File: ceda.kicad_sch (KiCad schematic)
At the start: 6 parts

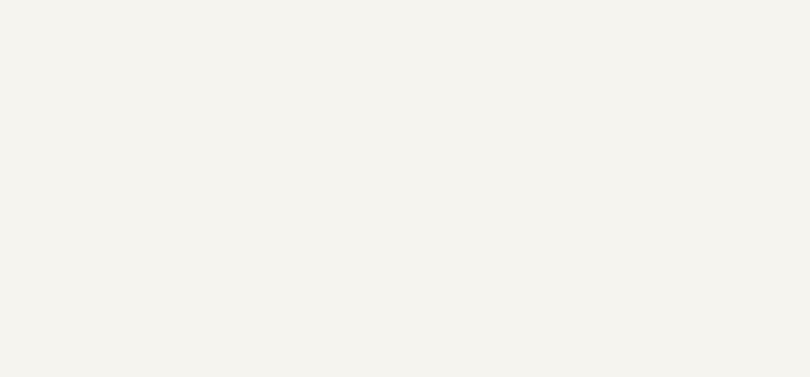
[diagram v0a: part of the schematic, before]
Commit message: CEDA symbol library: CRTC and uPD446.
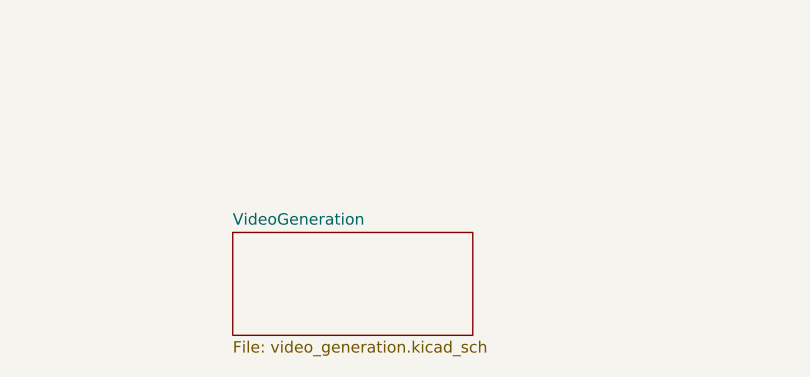
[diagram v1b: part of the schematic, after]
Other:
- added sheet VideoGeneration (video_generation.kicad_sch)
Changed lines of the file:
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@@
     (pin "2")
+  )
+  (sheet (at 36.83 153.67) (size 26.67 11.43) (fields_autoplaced)
+    (stroke (width 0.1524) (type solid) (color 0 0 0 0))
+    (fill (color 0 0 0 0.0000))
+    (property "Sheet name" "VideoGeneration" (id 0) (at 36.83 152.9584 0)
+      (effects (font (size 1.27 1.27)) (justify left bottom))
+    )
+    (property "Sheet file" "video_generation.kicad_sch" (id 1) (at 36.83 165.6846 0)
+      (effects (font (size 1.27 1.27)) (justify left top))
+    )
   )
   (sheet_instances
     (path "/" (page "1"))
+    (path "/ce60e45b-d802-4380-8f39-bef3de5fa20e" (page "2"))
   )
   (symbol_instances
+    (path "/ce60e45b-d802-4380-8f39-bef3de5fa20e/01062940-a891-466d-beec-dde8d3e3477c"
+      (reference "#PWR?") (unit 1) (value "VCC") (footprint "")
+    )
+    (path "/ce60e45b-d802-4380-8f39-bef3de5fa20e/16df3e84-7aac-4a70-983a-ea80cc491276"
+      (reference "#PWR?") (unit 1) (value "VCC") (footprint "")
+    )
     (path "/1c28d9b8-25c7-4d2d-9489-0dfc0748287c"
       (reference "#PWR?") (unit 1) (value "+5V") (footprint "")
@@
       (reference "D14") (unit 4) (value "74LS32") (footprint "")
     )
+    (path "/ce60e45b-d802-4380-8f39-bef3de5fa20e/614c8f87-26e6-4936-ac08-17824aabdbfb"
+      (reference "E7E11") (unit 1) (value "CRTC") (footprint "")
+    )
+    (path "/ce60e45b-d802-4380-8f39-bef3de5fa20e/94937845-9dc5-4c1c-85a4-ab12c8bbf530"
+      (reference "E13") (unit 1) (value "74LS04") (footprint "")
+    )
+    (path "/ce60e45b-d802-4380-8f39-bef3de5fa20e/24d193cd-79a4-4ad8-8472-2b96f466d141"
+      (reference "E13") (unit 4) (value "74LS04") (footprint "")
+    )
+    (path "/ce60e45b-d802-4380-8f39-bef3de5fa20e/a29b7863-01dd-4a76-a1d3-fb3b2966176c"
+      (reference "H8H10") (unit 1) (value "uPD446") (footprint "")
+    )
+    (path "/ce60e45b-d802-4380-8f39-bef3de5fa20e/22b6e0ee-3441-45f9-84ff-85d82c3fbd01"
+      (reference "J?") (unit 1) (value "Conn_02x05_Odd_Even") (footprint "")
+    )
     (path "/60d42a3c-6ebc-4e6b-b1fc-5783079f648c"
       (reference "J?") (unit 1) (value "Conn_02x25_Odd_Even") (footprint "")
@@
       (reference "JP?") (unit 1) (value "KB_SEL") (footprint "")
     )
+    (path "/ce60e45b-d802-4380-8f39-bef3de5fa20e/54526e8d-5138-4634-8385-27f827a36633"
+      (reference "L13") (unit 3) (value "74LS38") (footprint "")
+    )
+    (path "/ce60e45b-d802-4380-8f39-bef3de5fa20e/3a277ee5-8eca-46f5-92bf-31c4bb5c5405"
+      (reference "L13") (unit 4) (value "74LS38") (footprint "")
+    )
     (path "/e26c426b-0c90-469e-8f71-df4bc49765e0"
       (reference "R40") (unit 1) (value "4k7") (footprint "")
+    )
+    (path "/ce60e45b-d802-4380-8f39-bef3de5fa20e/f78a1727-4dfd-4dfe-b191-ba25a81f4c94"
+      (reference "R69") (unit 1) (value "470") (footprint "")
     )
     (path "/5ede8ab3-ae0a-43d9-8df9-d1279cb55cee"
       (reference "R79") (unit 1) (value "4k7") (footprint "")
     )
+    (path "/ce60e45b-d802-4380-8f39-bef3de5fa20e/35c8bfa7-9748-4a25-9a4c-b480bb3e2e54"
+      (reference "R?") (unit 1) (value "R") (footprint "")
+    )
   )

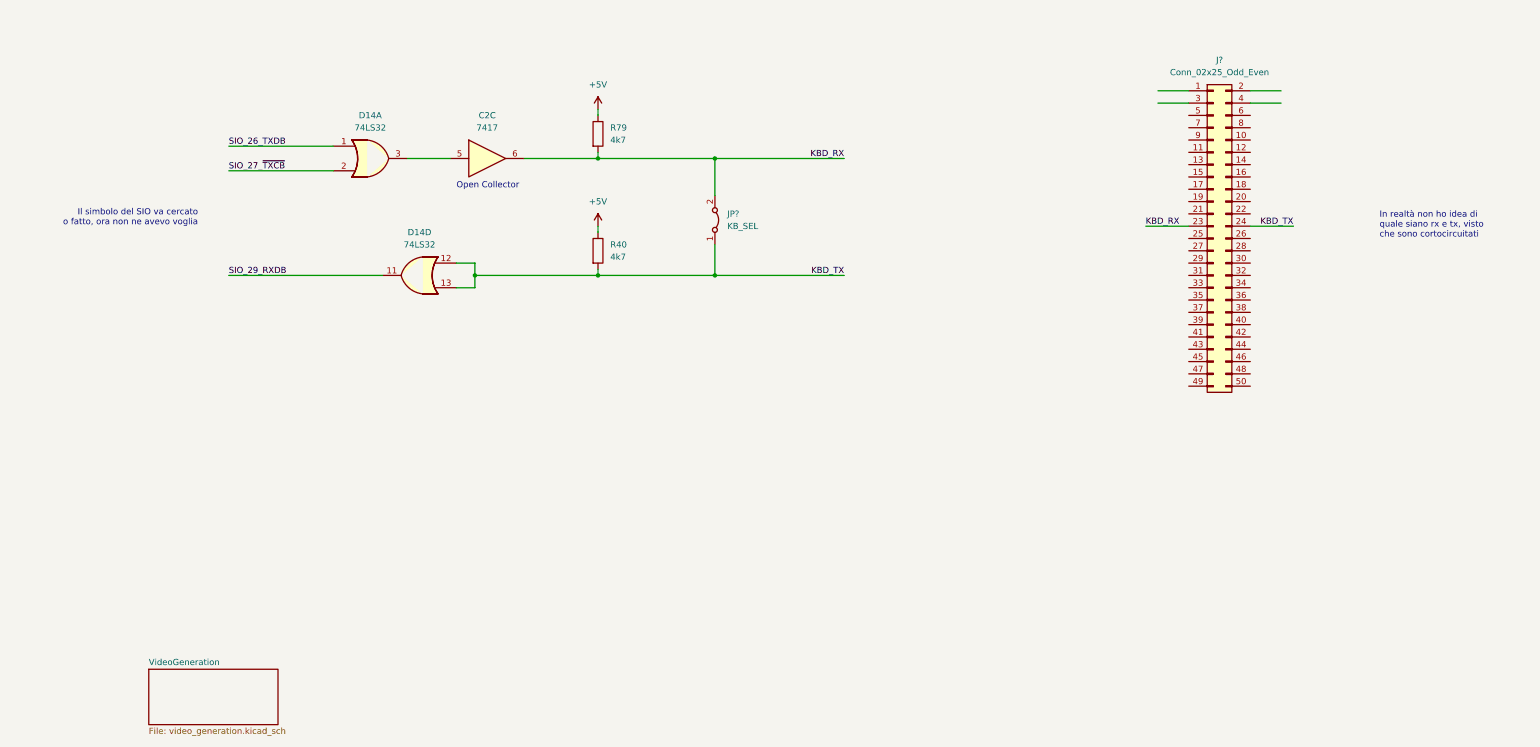
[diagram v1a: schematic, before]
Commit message: Moved keyboard circuit in its sheet
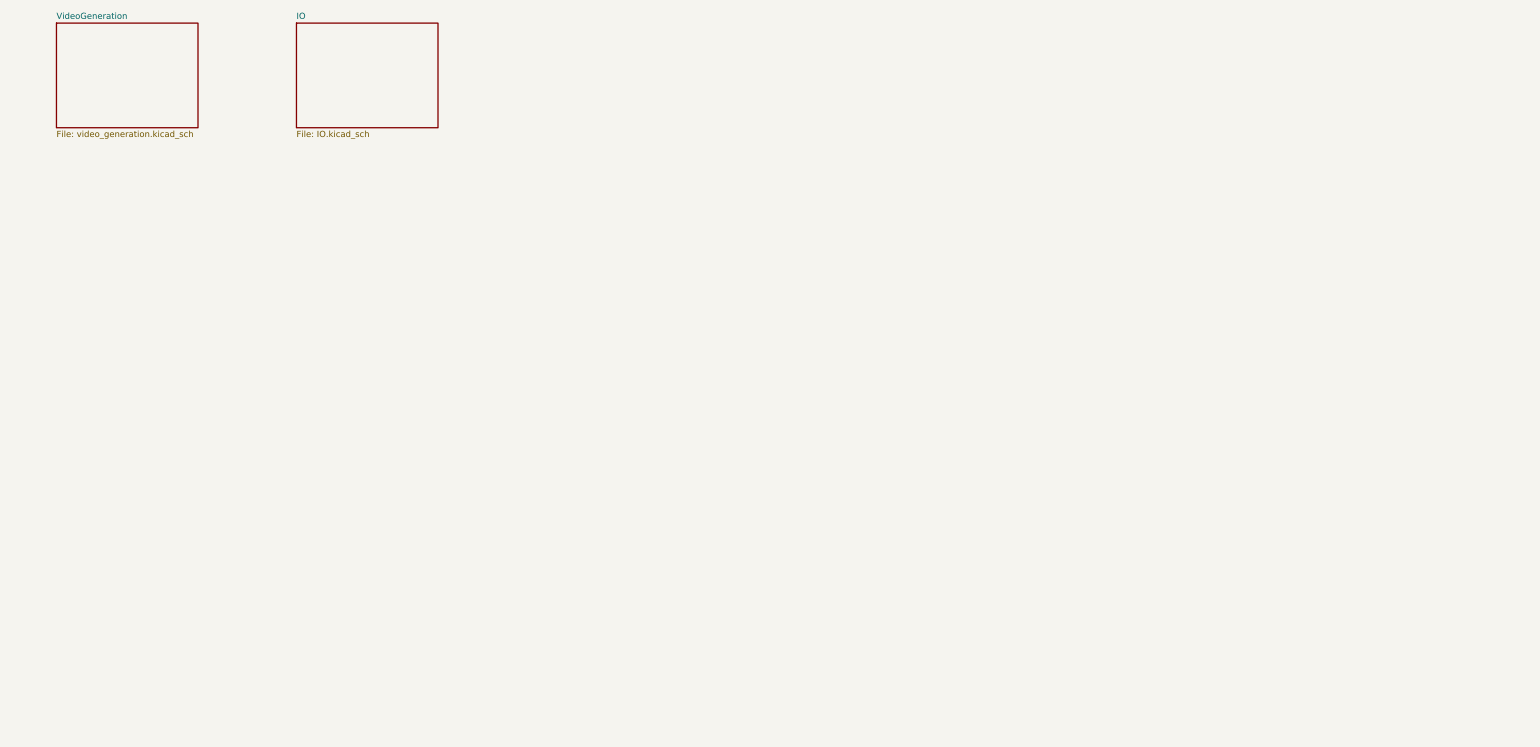
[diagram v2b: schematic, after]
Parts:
- removed C2: 7417, symbol 74xx:74LS07
- removed D14: 74LS32, symbol 74xx:74LS32
- removed J?: Conn_02x25_Odd_Even, symbol Connector_Generic:Conn_02x25_Odd_Even
- removed JP?: KB_SEL, symbol Jumper:Jumper_2_Bridged
- removed R40, R79: 4k7, symbol Device:R
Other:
- added sheet IO (IO.kicad_sch)
- note removed: "Il simbolo del SIO va cercato o fatto, ora non ne avevo voglia"
- note removed: "In realtà non ho idea di quale siano rx e tx, visto che sono cortocircuitati"
- note removed: "Open Collector"
- company: (none) -> Logic Systems Int'l Inc
- title: (none) -> FPX-290

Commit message: Update main project files.
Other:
- added sheet Speaker (speaker.kicad_sch)
- added sheet Z80CPU (z80cpu.kicad_sch)
